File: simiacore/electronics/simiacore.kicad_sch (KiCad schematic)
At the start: 32 parts, among them IC1 SN74HCS16507DR, J1 X_STEP_DRIVER, J10 Y1_LIM_PORT, J2 Y0_STEP_DRIVER, J3 Z_STEP_DRIVER, J4 Y1_STEP_DRIVER, J5 X_STEP, J6 X_LIM_PORT, J6 Y0_STEP, J7 Y0_LIM_PORT, J7 Z_STEP, J8 Y1_STEP, J8 Z_LIM_PORT, J9 SPINDLE_SPEED, SW1 LOGIC_TOGGLE, SW2 LOGIC_TOGGLE, SW3 LOGIC_TOGGLE, SW4 LOGIC_TOGGLE, U1 NCV20231XV53T2G, U3 PicoW

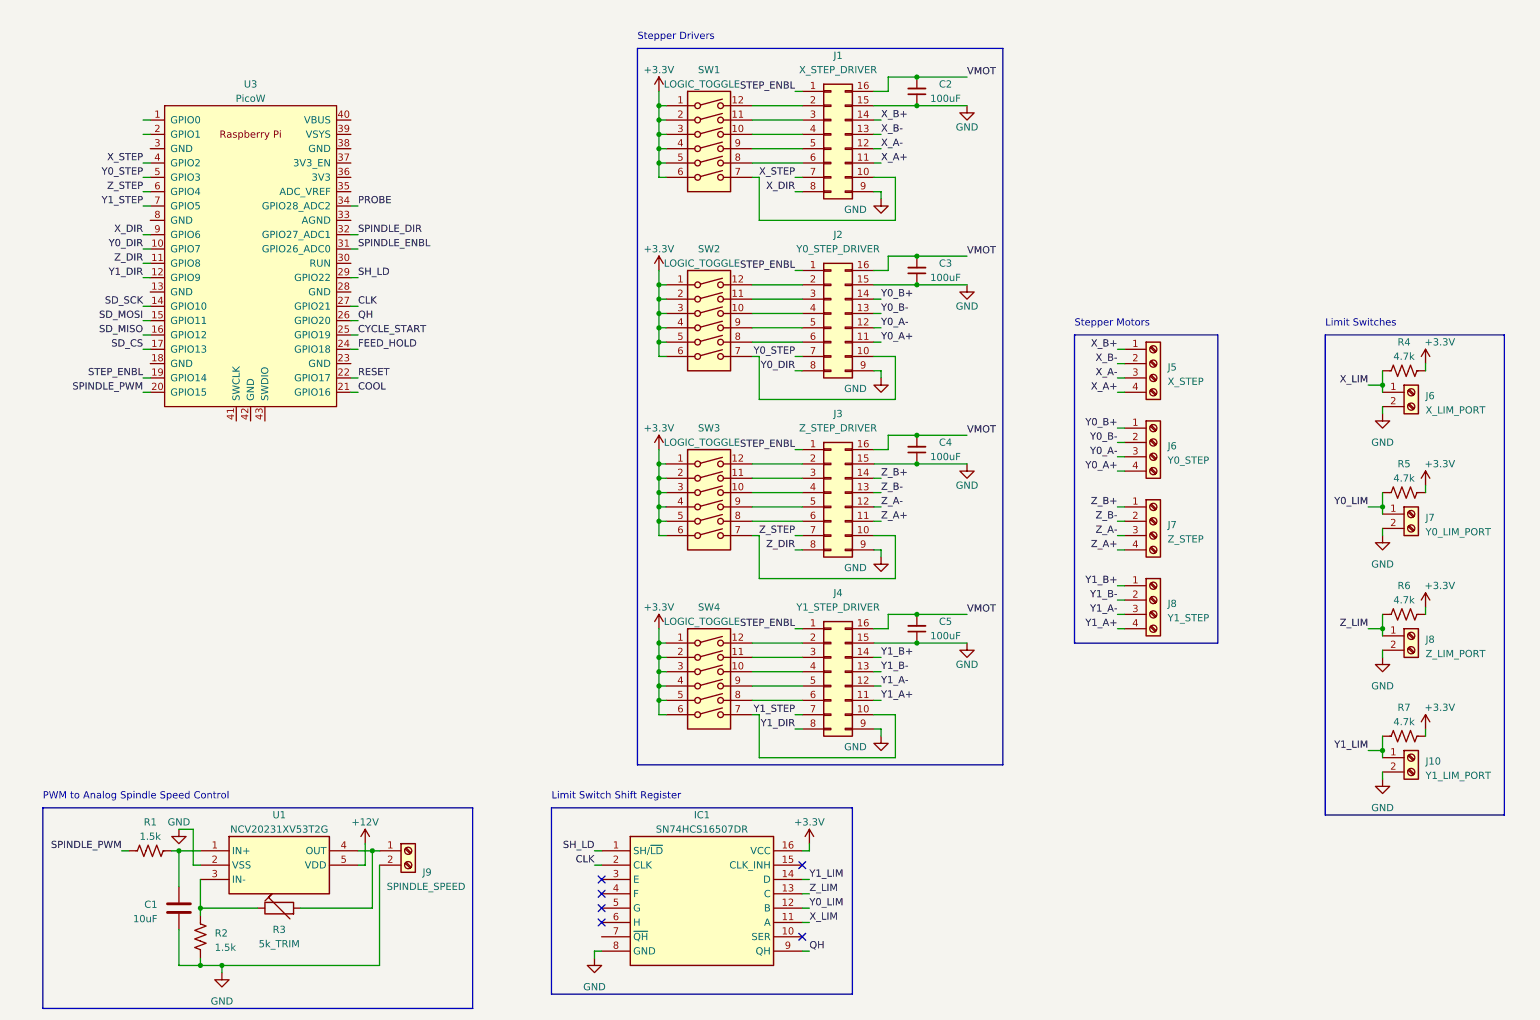
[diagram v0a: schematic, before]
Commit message: Fixed limit switch code
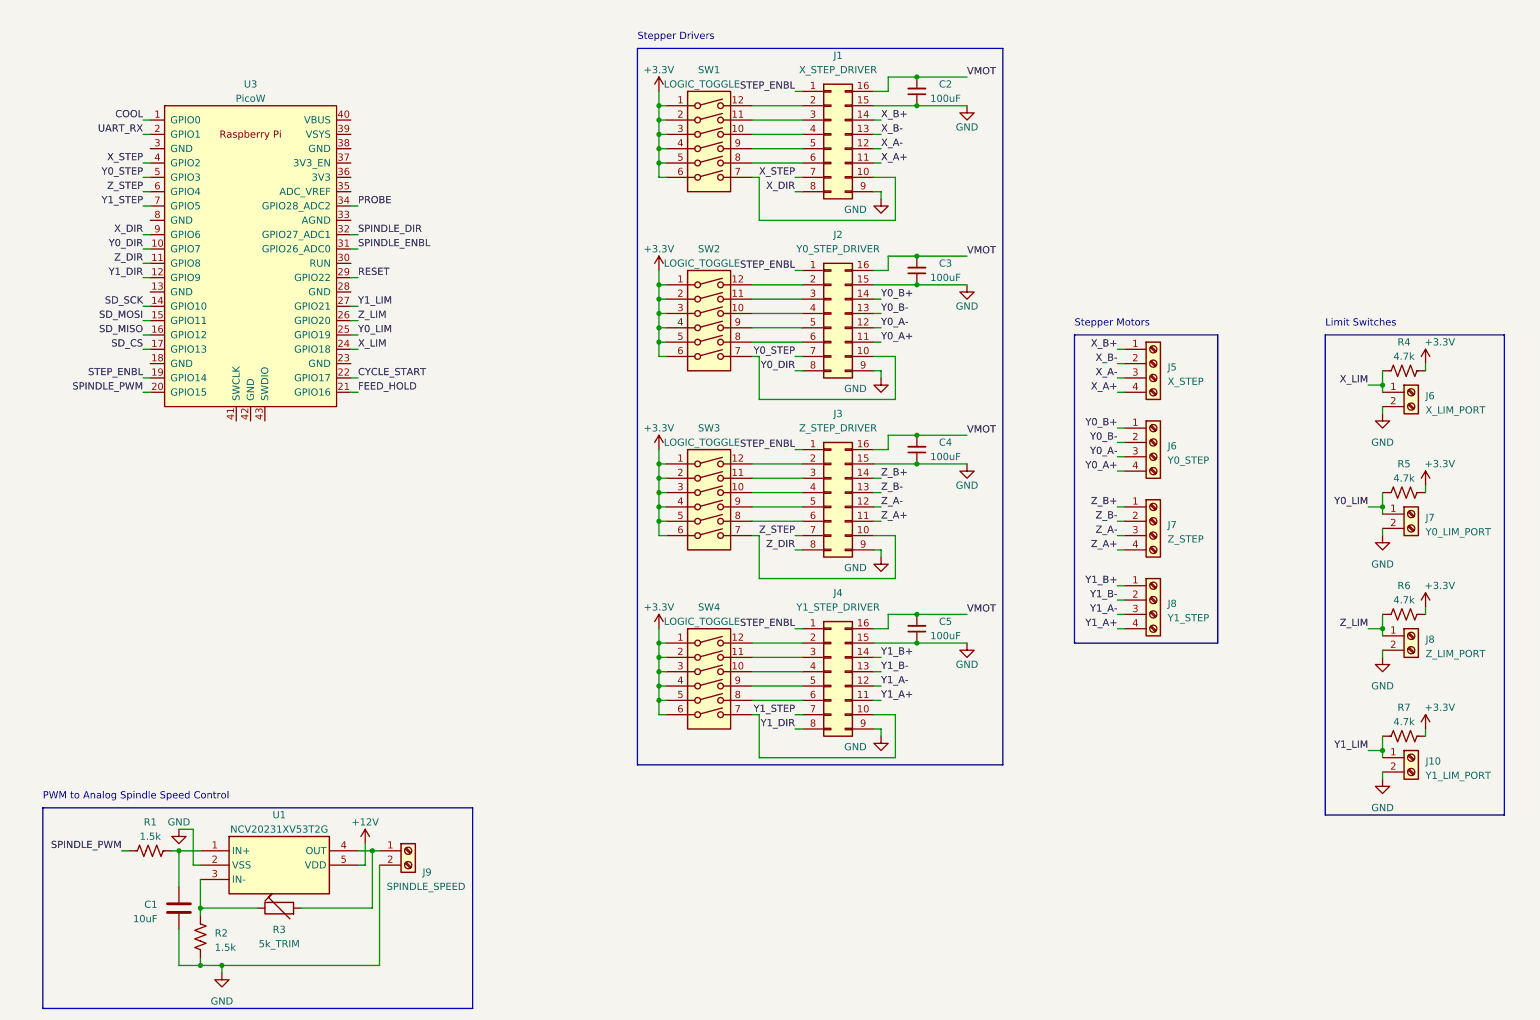
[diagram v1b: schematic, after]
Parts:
- removed IC1: SN74HCS16507DR, SOIC127P600X175-16N, symbol SamacSys_Parts:SN74HCS16507DR
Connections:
- net CLK is gone; now on net Y1_LIM: U3.27 (GPIO21)
- net QH is gone; now on net Z_LIM: U3.26 (GPIO20)
- net SH_LD is gone; now on net RESET: U3.29 (GPIO22)
- net COOL: now also U3.1 (GPIO0); no longer U3.21 (GPIO16)
- net CYCLE_START: now also U3.22 (GPIO17); no longer U3.25 (GPIO19)
- net FEED_HOLD: now also U3.21 (GPIO16); no longer U3.24 (GPIO18)
- net RESET: no longer U3.22 (GPIO17)
- net X_LIM: now also U3.24 (GPIO18)
- net Y0_LIM: now also U3.25 (GPIO19)
- net UART_RX: now reaches U3.2 (GPIO1)
- no-connect marks 6 -> 0
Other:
- note removed: "Limit Switch Shift Register"

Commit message: did some work
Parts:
- removed C2, C3, C4, C5: 100uF, mainboardlibrary:MAL203859101E3, symbol Device:C_Small
- removed J1: X_STEP_DRIVER, mainboardlibrary:16pinStepperDriverHeader, symbol Connector_Generic:Conn_02x08_Counter_Clockwise
- removed J2: Y0_STEP_DRIVER, mainboardlibrary:16pinStepperDriverHeader, symbol Connector_Generic:Conn_02x08_Counter_Clockwise
- removed J3: Z_STEP_DRIVER, mainboardlibrary:16pinStepperDriverHeader, symbol Connector_Generic:Conn_02x08_Counter_Clockwise
- removed J4: Y1_STEP_DRIVER, mainboardlibrary:16pinStepperDriverHeader, symbol Connector_Generic:Conn_02x08_Counter_Clockwise
- removed SW1, SW2, SW3, SW4: LOGIC_TOGGLE, mainboardlibrary:CFS-0600TB, symbol Switch:SW_DIP_x06
- removed U1: NCV20231XV53T2G, SOTFL50P160X60-5N, symbol SamacSys_Parts:NCV20231XV53T2G
- added J14: CYCLE_START_PORT, SamacSys_Parts:1190297, symbol Connector:Screw_Terminal_01x02
- added J15: FEED_HOLD_PORT, SamacSys_Parts:1190297, symbol Connector:Screw_Terminal_01x02
- added J16: 48VIN, SamacSys_Parts:1190297, symbol Connector:Screw_Terminal_01x02
- added R16, R17: 4.7k, SamacSys_Parts:RESC6432X65N, symbol Device:R
- added U2: NCS20231SN2T1G, SOT95P275X110-5N, symbol SamacSys_Parts:NCS20231SN2T1G
- J5, J6, J7, J8: footprint mainboardlibrary:1190299 -> SamacSys_Parts:1190299
- R1, R2, R4, R5, R6, R7: symbol Device:R_US -> Device:R
- U1: renamed from U3; footprint RPi_PicoW:RPi_Pico_SMD_TH -> RPi_Pico:RPi_PicoW_SMD_TH
- renumbered J7 to J10, J8 to J11, J10 to J12, J9 to J13, J6 to J9
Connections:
- net +12V: now also U2.5 (VDD)
- net +3.3V: now also U1.36 (3V3), R16.1, R17.1
- net CYCLE_START: now also J14.1 (Pin_1), R16.2
- net FEED_HOLD: now also J15.1 (Pin_1), R17.2
- net GND: now also J14.2 (Pin_2), J15.2 (Pin_2), U2.2 (VSS)
- net at R2.1, R3.1: now also U2.3 (IN+)
- net at C1.1, R1.2: now also U2.1 (OUT)
- net at J13.1 (Pin_1), R3.2: now also U2.4 (IN-)
- net +5V: now reaches U1.40 (VBUS)
- net X_A+ renamed Stepper Motor Drivers/X_B-
- net X_A- renamed Stepper Motor Drivers/X_B+
- net X_B+ renamed Stepper Motor Drivers/X_A+
- net X_B- renamed Stepper Motor Drivers/X_A-
- net Y0_A+ renamed Stepper Motor Drivers/Y0_B-
- net Y0_A- renamed Stepper Motor Drivers/Y0_B+
- net Y0_B+ renamed Stepper Motor Drivers/Y0_A+
- net Y0_B- renamed Stepper Motor Drivers/Y0_A-
- net Y1_A+ renamed Stepper Motor Drivers/Y1_B-
- net Y1_A- renamed Stepper Motor Drivers/Y1_B+
- net Y1_B+ renamed Stepper Motor Drivers/Y1_A+
- net Y1_B- renamed Stepper Motor Drivers/Y1_A-
- net Z_A+ renamed Stepper Motor Drivers/Z_B-
- net Z_A- renamed Stepper Motor Drivers/Z_B+
- net Z_B+ renamed Stepper Motor Drivers/Z_A+
- net Z_B- renamed Stepper Motor Drivers/Z_A-
- new net Power Delivery/GND: J16.2 (Pin_2)
- new net Power Delivery/VIN: J16.1 (Pin_1)
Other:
- added sheet MicroSD Slot (sd.kicad_sch)
- added sheet Power Delivery (power.kicad_sch)
- added sheet Stepper Motor Drivers (stepdrivers.kicad_sch)
- note removed: "Stepper Drivers"
- moved on the sheet: C1, J10, J11, J12, J13, J5, J6, J7, J8, J9, R3, U1
